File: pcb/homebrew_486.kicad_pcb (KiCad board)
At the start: 4 copper layers, 150 x 150 mm, 159 parts, among them J1 Bus_ISA_16bit, J11 PEN, J13 KB, J15 PC SPK, J16 ATUART, J18 EXT. RESET, J19 Conn_01x02_Pin, J2 Bus_ISA_16bit, J20 Conn_01x02_Pin, J21 Conn_01x02_Pin, J22 Conn_01x02_Pin, J3 ATX-20, J4 AVR ISP, J5 Cmos settings, J6 Enable load, J9 x2 Multiplier, SW1 SW_SPDT, SW2 Reset, U1 486Socket, U10 8259A-2, U11 HM628512, U12 HM628512, U13 HM628512, U14 HM628512, U15 HM628512, U16 HM628512, U17 HM628512, U18 HM628512, U19 74LS245, U2 XC2S100TQ144, U20 74LS245, U21 W29C020, U22 ATmega128L-8A, U3 AMS1117, U4 AMS1117, U5 74LS245, U6 74LS245, U7 74LS245, U8 74LS245, U9 8254, Y1 TXC-7C, Y2 GTXO-14T, Y3 16MHz

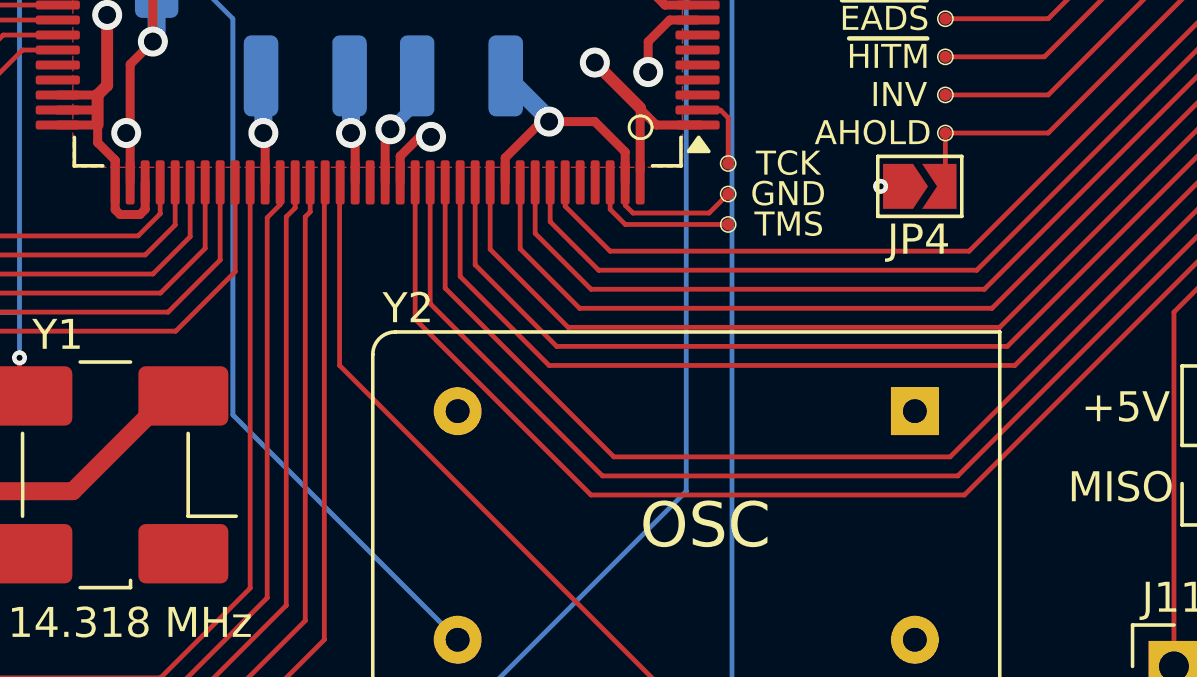
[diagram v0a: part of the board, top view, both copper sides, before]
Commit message: few more free IO pads exposed
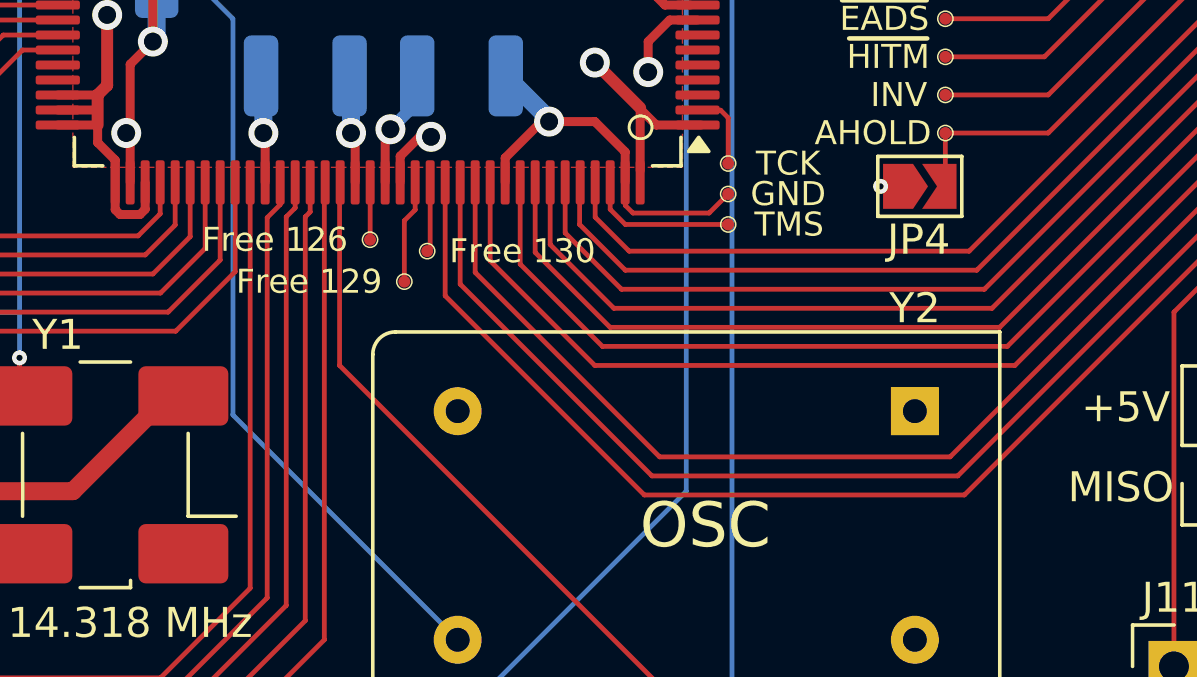
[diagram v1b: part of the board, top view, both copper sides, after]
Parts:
- added TP15: Free 126, 486custom:TestPoint_Pad_D0.4mm, F.Cu at (75.4, 152.8)
- added TP16: Free 130, 486custom:TestPoint_Pad_D0.4mm, F.Cu at (77.3, 153.2)
- added TP17: Free 129, 486custom:TestPoint_Pad_D0.4mm, F.Cu at (76.6, 154.2)
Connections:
- U2 pad 126: unconnected-(U2-IO/TRDY-Pad126) -> Net-(TP15-Pad1)
- U2 pad 129: /FPGA/~{RAM_OE_B3} -> Net-(TP17-Pad1)
- U2 pad 130: /FPGA/~{RAM_OE_B2} -> Net-(TP16-Pad1)
- U2 pad 131: /FPGA/~{RAM_OE_B1} -> /FPGA/~{RAM_OE_B3}
- U2 pad 132: /FPGA/~{RAM_OE_B0} -> /FPGA/~{RAM_OE_B2}
- U2 pad 133: /FPGA/~{RAM_WE_B3} -> /FPGA/~{RAM_OE_B1}
- U2 pad 134: /FPGA/~{RAM_WE_B2} -> /FPGA/~{RAM_OE_B0}
- U2 pad 136: /FPGA/~{RAM_WE_B1} -> /FPGA/~{RAM_WE_B3}
- U2 pad 137: /FPGA/~{RAM_WE_B0} -> /FPGA/~{RAM_WE_B2}
- U2 pad 138: /~{RAM_CS0} -> /FPGA/~{RAM_WE_B1}
- U2 pad 139: /~{RAM_CS1} -> /FPGA/~{RAM_WE_B0}
- U2 pad 140: unconnected-(U2-IO-Pad140) -> /~{RAM_CS0}
- U2 pad 141: unconnected-(U2-IO-Pad141) -> /~{RAM_CS1}
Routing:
- net Net-(TP17-Pad1): track 0.00 -> 3.46 mm
- net Net-(TP16-Pad1): track 0.00 -> 2.33 mm
- net Net-(TP15-Pad1): track 0.00 -> 1.91 mm
- net /FPGA/~{RAM_WE_B3}: track 215.6 -> 214.1 mm
- net /FPGA/~{RAM_OE_B3}: track 206.8 -> 205.3 mm
- net /FPGA/~{RAM_WE_B2}: track 188.4 -> 186.9 mm
- net /FPGA/~{RAM_OE_B2}: track 180.0 -> 178.6 mm
- net /FPGA/~{RAM_OE_B1}: track 152.6 -> 151.3 mm
- net /FPGA/~{RAM_OE_B0}: track 116.8 -> 115.5 mm
- net /FPGA/~{RAM_WE_B1}: track 161.7 -> 160.6 mm
- net /FPGA/~{RAM_WE_B0}: track 134.7 -> 133.7 mm
- net /~{RAM_CS0}: track 220.8 -> 219.9 mm
- net /~{RAM_CS1}: track 182.9 -> 182.1 mm

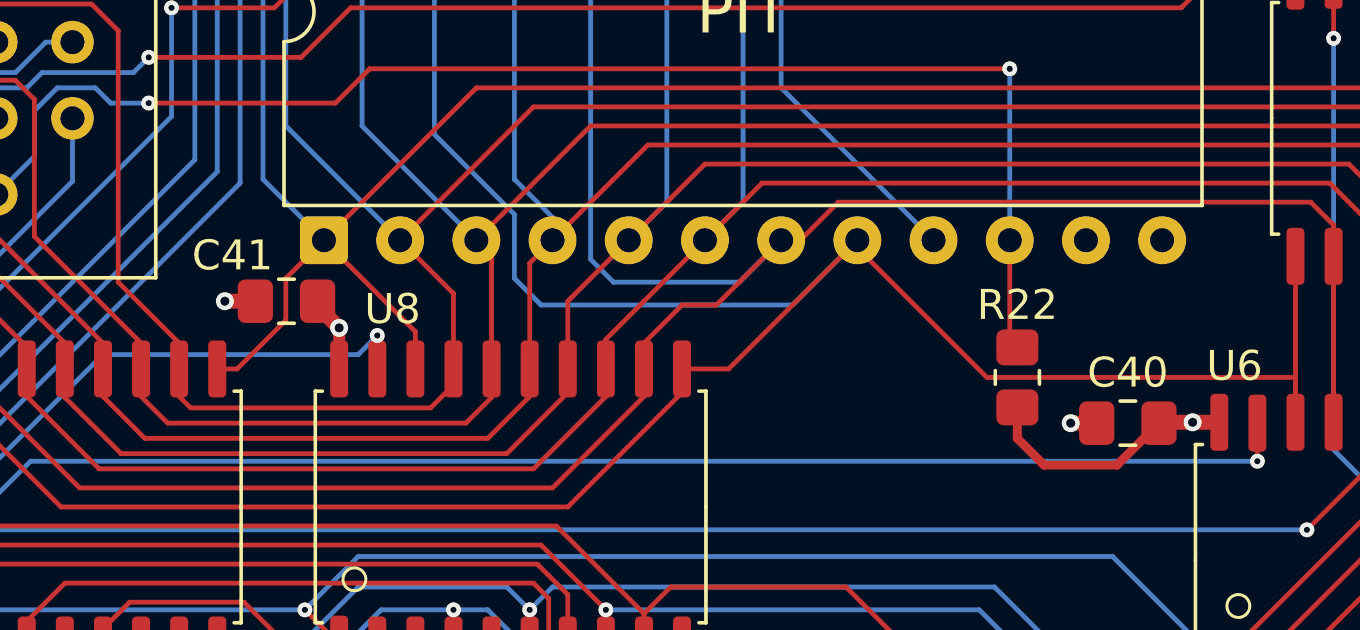
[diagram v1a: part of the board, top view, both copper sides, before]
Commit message: data_bus_tr paired up, correct decoupling caps per pair
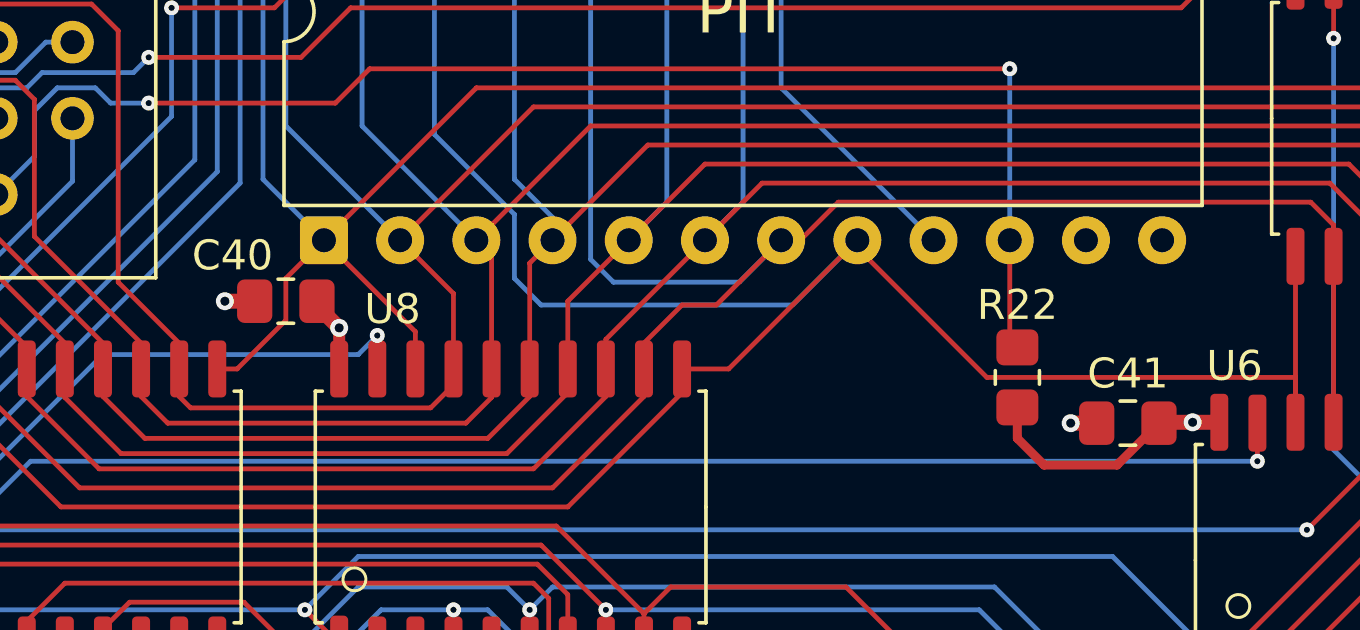
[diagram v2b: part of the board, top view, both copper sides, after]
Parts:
- moved C40 28.4 mm to (84.3, 62.2)
- moved C41 28.3 mm to (112.4, 66.3)
